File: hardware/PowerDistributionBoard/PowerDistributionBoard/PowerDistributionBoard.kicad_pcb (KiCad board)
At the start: 4 copper layers, 180 x 120 mm, 96 parts, among them J1 Battery, J10 ESC2_PWR, J2 FAN 1, J3 FAN 2, J4 FAN 3, J5 FAN 4, J6 Inverter, J7 Control Board, J8 Conn_01x02, J9 ESC1_PWR, K1 J115F11AH12VDCS61.5, K2 J115F11AH12VDCS61.5, Q1 Q_NMOS_GDS, Q2 Q_NPN_EBC, Q3 Q_NMOS_GSD, Q4 Q_NMOS_GSD, Q5 Q_NPN_EBC, Q6 Q_NMOS_GSD, Q7 Q_NMOS_GSD, Q8 Q_NPN_BEC, SW1 SW_SPDT, U1 LT1641-1, U2 MAX6643LBBAEET, U3 MAX6643LBBAEET, U4 MC74HC20ADG, U5 KSTW004A2B41Z, U6 AP2210N-3.3TRG1

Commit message: Motor Control with ESP/Estop
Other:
- board text added: "OFF"
- board text added: "ON"
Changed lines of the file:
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@@
       (layer "F.Paste" (type "Top Solder Paste"))
       (layer "F.Mask" (type "Top Solder Mask") (thickness 0.01))
-      (layer "F.Cu" (type "copper") (thickness 0.0681))
-      (layer "dielectric 1" (type "core") (thickness 0.469866) (material "FR4") (epsilon_r 4.5) (loss_tangent 0.02))
-      (layer "In1.Cu" (type "copper") (thickness 0.0171))
-      (layer "dielectric 2" (type "prepreg") (thickness 0.469866) (material "FR4") (epsilon_r 4.5) (loss_tangent 0.02))
-      (layer "In2.Cu" (type "copper") (thickness 0.0171))
-      (layer "dielectric 3" (type "core") (thickness 0.469866) (material "FR4") (epsilon_r 4.5) (loss_tangent 0.02))
-      (layer "B.Cu" (type "copper") (thickness 0.0681))
+      (layer "F.Cu" (type "copper") (thickness 0.07))
+      (layer "dielectric 1" (type "core") (thickness 0.456666) (material "FR4") (epsilon_r 4.5) (loss_tangent 0.02))
+      (layer "In1.Cu" (type "copper") (thickness 0.035))
+      (layer "dielectric 2" (type "prepreg") (thickness 0.456666) (material "FR4") (epsilon_r 4.5) (loss_tangent 0.02))
+      (layer "In2.Cu" (type "copper") (thickness 0.035))
+      (layer "dielectric 3" (type "core") (thickness 0.456666) (material "FR4") (epsilon_r 4.5) (loss_tangent 0.02))
+      (layer "B.Cu" (type "copper") (thickness 0.07))
       (layer "B.Mask" (type "Bottom Solder Mask") (thickness 0.01))
       (layer "B.Paste" (type "Bottom Solder Paste"))
@@
       (rotate (xyz 0 0 0))
     )
+    (model "${KIPRJMOD}/Parts/3D Models/436500215.stp"
+      (offset (xyz 1.5 1.9 10))
+      (scale (xyz 1 1 1))
+      (rotate (xyz 90 0 180))
+    )
   )
   (footprint "Resistor_SMD:R_0805_2012Metric" (layer "F.Cu")
@@
       (net 2 "GND") (pinfunction "Pin_2") (pintype "passive"))
     (model "${KICAD6_3DMODEL_DIR}/Connector_Molex.3dshapes/Molex_Mini-Fit_Sr_42820-22XX_1x02_P10.00mm_Horizontal.wrl"
-      (offset (xyz 0 0 0))
+      (offset (xyz 17.25 -5 6.5))
       (scale (xyz 1 1 1))
-      (rotate (xyz 0 0 0))
+      (rotate (xyz -90 0 -90))
+    )
+    (model "${KIPRJMOD}/Parts/3D Models/428202223--3DModel-STEP-390490.STEP"
+      (offset (xyz 17.25 -5 6.5))
+      (scale (xyz 1 1 1))
+      (rotate (xyz -90 0 -90))
     )
   )
@@
     (effects (font (size 1.5 1.5) (thickness 0.3)))
   )
+  (gr_text "ON\n" (at 42.275 84.7) (layer "F.SilkS")
+    (effects (font (size 1 1) (thickness 0.15)))
+  )
   (gr_text "Paradigm IGVC\nPower Distribution Board Rev 1\nDylan Matthews 2023" (at 134.6 44.525) (layer "F.SilkS")
     (effects (font (size 1.5 1.5) (thickness 0.3)))
@@
     (effects (font (size 1.5 1.5) (thickness 0.3)))
   )
+  (gr_text "OFF" (at 42.2 89.925) (layer "F.SilkS")
+    (effects (font (size 1 1) (thickness 0.15)))
+  )
   (gr_text "FANS" (at 183.85 26.5) (layer "F.SilkS")

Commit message: More Control Board Routing Stuff
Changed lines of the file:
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@@
       (effects (font (size 1 1) (thickness 0.15)))
     )
-    (fp_line (start 8 4.5) (end -8 4.5) (layer "F.SilkS") (width 0.12))
-    (fp_line (start -8 -4.5) (end 8 -4.5) (layer "F.SilkS") (width 0.12))
-    (fp_line (start -8 4.5) (end -8 -4.5) (layer "F.SilkS") (width 0.12))
-    (fp_line (start 8 -4.5) (end 8 4.5) (layer "F.SilkS") (width 0.12))
-    (pad "1" smd roundrect (at -5.4 0 180) (size 4.5 8) (layers "F.Cu" "F.Paste" "F.Mask") (roundrect_rratio 0.25)
+    (fp_line (start 8.1 -4.5) (end 8.1 4.5) (layer "F.SilkS") (width 0.12))
+    (fp_line (start 8.1 4.5) (end -8.1 4.5) (layer "F.SilkS") (width 0.12))
+    (fp_line (start -8.1 4.5) (end -8.1 -4.5) (layer "F.SilkS") (width 0.12))
+    (fp_line (start -8.1 -4.5) (end 8.1 -4.5) (layer "F.SilkS") (width 0.12))
+    (pad "1" smd rect (at -5.4 0 180) (size 5.2 8.75) (layers "F.Cu" "F.Paste" "F.Mask")
       (net 28 "Net-(Q1-Pad2)") (pintype "passive"))
-    (pad "2" smd roundrect (at 5.4 0 180) (size 4.5 8) (layers "F.Cu" "F.Paste" "F.Mask") (roundrect_rratio 0.25)
+    (pad "2" smd rect (at 5.4 0 180) (size 5.2 8.75) (layers "F.Cu" "F.Paste" "F.Mask")
       (net 3 "/BATT_RAW") (pintype "passive"))
   )
@@
     (property "Sheetname" "")
     (attr smd)
-    (fp_text reference "Q1" (at 0 -6.65 90) (layer "F.SilkS")
+    (fp_text reference "Q1" (at 9.625 -0.8) (layer "F.SilkS")
       (effects (font (size 1 1) (thickness 0.15)))
     )
@@
         (xy 67.075 77.025)
         (xy 67.101986 80.877896)
-        (xy 59.401986 80.977896)
-        (xy 59.4 67.75)
+        (xy 59.351712 80.977903)
+        (xy 59.349726 67.750007)
         (xy 72.375 57.425)
         (xy 80.563965 57.427856)

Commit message: PDB Layout
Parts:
- removed K1, K2: J115F11AH12VDCS61.5, PDBLib:J115F11AH12VDCS61.5
- added C18: 1u, Capacitor_SMD:C_0805_2012Metric, F.Cu at (85.8, 79.3)
- added C19: 10u, Capacitor_SMD:C_0805_2012Metric, F.Cu at (181.2, 63.2)
- added C20: 1u, Capacitor_SMD:C_0805_2012Metric, F.Cu at (179.1, 63.2)
- added C21: 220uF, Capacitor_THT:CP_Radial_D6.3mm_P2.50mm, F.Cu at (162.6, 59.8)
- added C22: 1u, Capacitor_SMD:C_0805_2012Metric, F.Cu at (179.1, 66.7)
- added C23: 10u, Capacitor_SMD:C_0805_2012Metric, F.Cu at (181.2, 66.7)
- added D10: D, PDBLib:VS-15AWL06FNTR-M3, F.Cu at (182.6, 91.4)
- added D11: S1G, Diode_SMD:D_SMA, F.Cu at (76.6, 115.2)
- added D12: S1G, Diode_SMD:D_SMA, F.Cu at (125.8, 35.4)
- added D13: S1G, Diode_SMD:D_SMA, F.Cu at (209.7, 66.3)
- added D8: S1G, Diode_SMD:D_SMA, F.Cu at (172.7, 34.0)
- added D9: D, PDBLib:VS-15AWL06FNTR-M3, F.Cu at (138.9, 107.7)
- added F2: 10A, PDBLib:3557-2, F.Cu at (143.8, 91.9)
- added F3: 25A, PDBLib:3557-2, F.Cu at (97.7, 110.8)
- added F4: 2A, PDBLib:3557-2, F.Cu at (143.6, 40.2)
- added F5: 10A, PDBLib:3557-2, F.Cu at (167.1, 86.8)
- added F6: 1A, PDBLib:3557-2, F.Cu at (194.6, 66.0)
- added J11: Router, Connector_Molex:Molex_Micro-Fit_3.0_43650-0215_1x02_P3.00mm_Vertical, F.Cu at (217.0, 64.8)
- added Q10: TK100E10N1,S1X, Package_TO_SOT_THT:TO-220-3_Vertical, F.Cu at (164.3, 101.2)
- added Q9: TK100E10N1,S1X, Package_TO_SOT_THT:TO-220-3_Vertical, F.Cu at (119.4, 107.9)
- added R36: 1k, Resistor_SMD:R_0805_2012Metric, F.Cu at (119.4, 116.7)
- added R37: 0, Resistor_SMD:R_2512_6332Metric, F.Cu at (127.5, 105.3)
- added R38: 0, Resistor_SMD:R_2512_6332Metric, F.Cu at (134.9, 98.2)
- added R39: 1k, Resistor_SMD:R_0805_2012Metric, F.Cu at (164.3, 108.0)
- added R40: 0, Resistor_SMD:R_2512_6332Metric, F.Cu at (173.2, 95.5)
- added R41: 0, Resistor_SMD:R_2512_6332Metric, F.Cu at (176.1, 102.3)
- added R42: 100, Resistor_SMD:R_0805_2012Metric, F.Cu at (50.5, 89.7)
- added R43: 100, Resistor_SMD:R_0805_2012Metric, F.Cu at (75.6, 85.3)
- added R44: 4.7k, Resistor_SMD:R_0805_2012Metric, F.Cu at (177.4, 129.7)
- added U7: R-78B9.0-1.0, PDBLib:R-78B9.0-1.0, F.Cu at (171.8, 65.0)
- C1: value 0.68u -> 68n
- C17, C9: footprint Capacitor_THT:CP_Radial_D12.5mm_P5.00mm -> Capacitor_THT:CP_Radial_D10.0mm_P5.00mm
- C3: value 10n -> 1n
- C4: value 1000u -> 220u; footprint Capacitor_THT:CP_Radial_D18.0mm_P7.50mm -> Capacitor_THT:CP_Radial_D16.0mm_P7.50mm
- D2: value D -> SML-P11UTT86R; footprint Diode_SMD:D_SMA -> LED_SMD:LED_0402_1005Metric
- D3: value D -> S1G
- D4, D5: value D -> S1G; footprint Package_TO_SOT_THT:TO-247-2_Horizontal_TabDown -> Diode_SMD:D_SMA
- F1: footprint PDBLib:0679L1000-05 -> PDBLib:3557-2
- J10: value ESC2_PWR -> MOTOR2_PWR
- J7: footprint Connector_Molex:Molex_Micro-Fit_3.0_43650-0200_1x02_P3.00mm_Horizontal -> Connector_Molex:Molex_Micro-Fit_3.0_43650-0215_1x02_P3.00mm_Vertical
- J9: value ESC1_PWR -> MOTOR1_PWR
- Q8: value Q_NPN_BEC -> DMN62D0U-13; footprint Package_TO_SOT_SMD:SOT-23 -> PDBLib:DMN62D0U-13
- R17, R18, R21, R22: value DNP -> 0
- R25: value 360 -> 3.4k
- R3: value 48k -> 46.4k
- R33: value 3k -> 4.7k
- R34: value 0 -> 330
- R35: value DNP -> 1k
- R4: value 0.75m -> 1m
- TP1: value TestPoint -> ON
- TP3: value TestPoint -> ESTOP
- TP4: value TestPoint -> +12V
- moved D3 102.8 mm to (160.9, 34.0), turned to 180 degrees
- moved G*** 95.9 mm to (108.5, 133.5)
- moved J8 93.0 mm to (185.1, 128.8), turned to 90 degrees
- moved D4 92.5 mm to (191.2, 34.0), turned to 180 degrees
- moved TP3 77.0 mm to (180.1, 128.8), turned to 90 degrees
- moved R33 76.9 mm to (175.1, 127.8), turned to 90 degrees
- moved D5 64.6 mm to (203.2, 34.0), turned to 180 degrees
- moved R34 59.7 mm to (171.8, 128.7)
- moved Q8 59.2 mm to (167.6, 127.8), turned to 90 degrees
- moved D2 55.0 mm to (61.0, 89.8), turned to 0 degrees
- moved R35 51.9 mm to (164.3, 128.7), turned to -90 degrees
- moved J9 48.3 mm to (143.7, 116.9), turned to -90 degrees
- moved R25 48.0 mm to (62.1, 92.4), turned to -90 degrees
- moved C16 35.4 mm to (83.7, 79.3)
- moved J7 21.9 mm to (117.7, 36.8), turned to 90 degrees
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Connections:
- net /FAN_FAIL1 renamed /FAN_FAIL1_N
- net /FAN_FAIL2 renamed /FAN_FAIL2_N
- net /OVERTEMP1 renamed /OVERTEMP1_N
- net /OVERTEMP2 renamed /OVERTEMP2_N
- C16 pad 1: /ESTOP -> GND
- C16 pad 2: GND -> +48V
- C17 pad 1: +48V -> Net-(D11-Pad1)
- D1 pad 2: +48V -> Net-(D1-Pad2)
- D2 pad 1: +12V -> Net-(D2-Pad1)
- D2 pad 2: Net-(D2-Pad2) -> /BATT_GOOD
- D3 pad 2: Net-(D2-Pad2) -> Net-(D3-Pad2)
- D4 pad 1: /ESC1_PWR -> +12V
- D4 pad 2: GND -> Net-(D4-Pad2)
- D5 pad 1: /ESC2_PWR -> +12V
- D5 pad 2: GND -> Net-(D5-Pad2)
- F1 pad 1: +48V -> Net-(C9-Pad1)
- F1 pad 2: Net-(C9-Pad1) -> +48V
- J10 pad 1: /ESC2_PWR -> Net-(D10-Pad1)
- J10 pad 2: GND -> Net-(D10-Pad2)
- J2 pad 1: Net-(J2-Pad1) -> Net-(D4-Pad2)
- J3 pad 1: Net-(J3-Pad1) -> Net-(D5-Pad2)
- J4 pad 1: Net-(J4-Pad1) -> Net-(D3-Pad2)
- J5 pad 1: Net-(J5-Pad1) -> Net-(D8-Pad2)
- J6 pad 1: +48V -> Net-(D11-Pad1)
- J7 pad 1: +12V -> Net-(D12-Pad1)
- J8 pad 1: Net-(J8-Pad1) -> /ESTOP
- J9 pad 1: /ESC1_PWR -> Net-(D9-Pad1)
- J9 pad 2: GND -> Net-(D9-Pad2)
- Q8 pad 3: Net-(Q8-Pad3) -> /MOTOR_FET_GATE
- R17 pad 1: Net-(J2-Pad1) -> GND
- R17 pad 2: GND -> Net-(D4-Pad2)
- R18 pad 1: Net-(J4-Pad1) -> GND
- R18 pad 2: GND -> Net-(D3-Pad2)
- R19 pad 1: Net-(J2-Pad1) -> Net-(D4-Pad2)
- R20 pad 1: Net-(J4-Pad1) -> Net-(D3-Pad2)
- R21 pad 1: Net-(J3-Pad1) -> GND
- R21 pad 2: GND -> Net-(D5-Pad2)
- R22 pad 1: Net-(J5-Pad1) -> GND
- R22 pad 2: GND -> Net-(D8-Pad2)
- R23 pad 1: Net-(J3-Pad1) -> Net-(D5-Pad2)
- R24 pad 1: Net-(J5-Pad1) -> Net-(D8-Pad2)
- R25 pad 1: Net-(Q8-Pad1) -> /BATT_GOOD
- R25 pad 2: /ESTOP -> GND
- R33 pad 2: Net-(J8-Pad1) -> +3V3
- R34 pad 1: Net-(Q8-Pad3) -> Net-(Q8-Pad1)
- R34 pad 2: Net-(D2-Pad2) -> /ESTOP
- R35 pad 1: GND -> /MOTOR_FET_GATE
- R35 pad 2: Net-(D2-Pad2) -> +12V
- SW1 pad 3: Net-(C14-Pad1) -> Net-(SW1-Pad3)
- U1 pad 3: /BATT_GOOD -> Net-(D2-Pad1)
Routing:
- net +12V: track 250.6 -> 12.3 mm
- net Net-(D2-Pad2): track 50.8 -> 0.00 mm
- net GND: track 104.4 -> 81.8 mm, vias 96 -> 53
- net /FAN_TACH4: track 21.2 -> 1.03 mm
- net /FAN_TACH2: track 21.0 -> 1.08 mm
- net /FAN_TACH1: track 19.5 -> 0.00 mm
- net /FAN_TACH3: track 19.7 -> 6.72 mm
- net Net-(Q3-Pad1): track 12.7 -> 0.00 mm
- net Net-(R14-Pad1): track 8.08 -> 0.00 mm
- net Net-(J5-Pad1): track 7.84 -> 0.00 mm
- net Net-(J4-Pad1): track 7.75 -> 0.00 mm
- net Net-(J3-Pad1): track 7.74 -> 0.00 mm
- net Net-(C14-Pad1): track 13.7 -> 5.99 mm
- net Net-(J2-Pad1): track 7.61 -> 0.00 mm
- net /ESTOP: track 7.27 -> 0.00 mm
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- removed copper zone on B.Cu, net +12V
- removed copper zone on F.Cu, net +12V
- removed copper zone on B.Cu, net /ESC1_PWR
- removed copper zone on F.Cu, net /ESC1_PWR
- removed copper zone on B.Cu, net /ESC2_PWR
- removed copper zone on F.Cu, net /ESC2_PWR
- removed copper zone on B.Cu, net Net-(C9-Pad1)
- removed copper zone on F.Cu, net Net-(C9-Pad1)
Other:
- board text removed: "CONTROL BOARD"
- board text removed: "ESC1 POWER"
- board text removed: "ESC2 POWER"

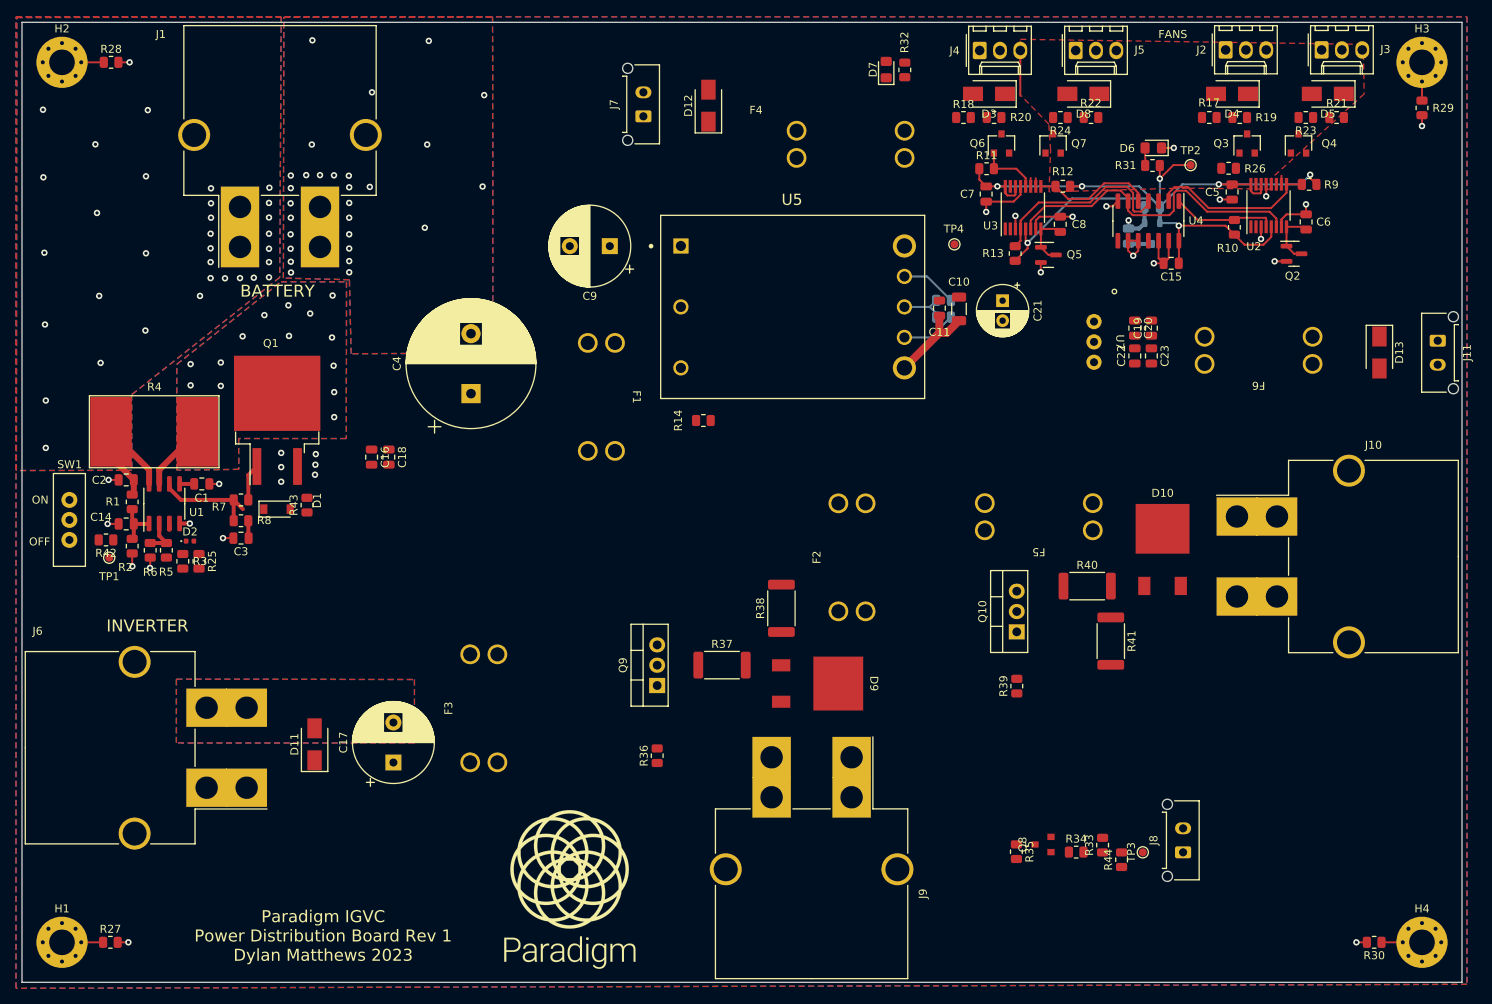
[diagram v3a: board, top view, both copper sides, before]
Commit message: PDB routing V2 first pass
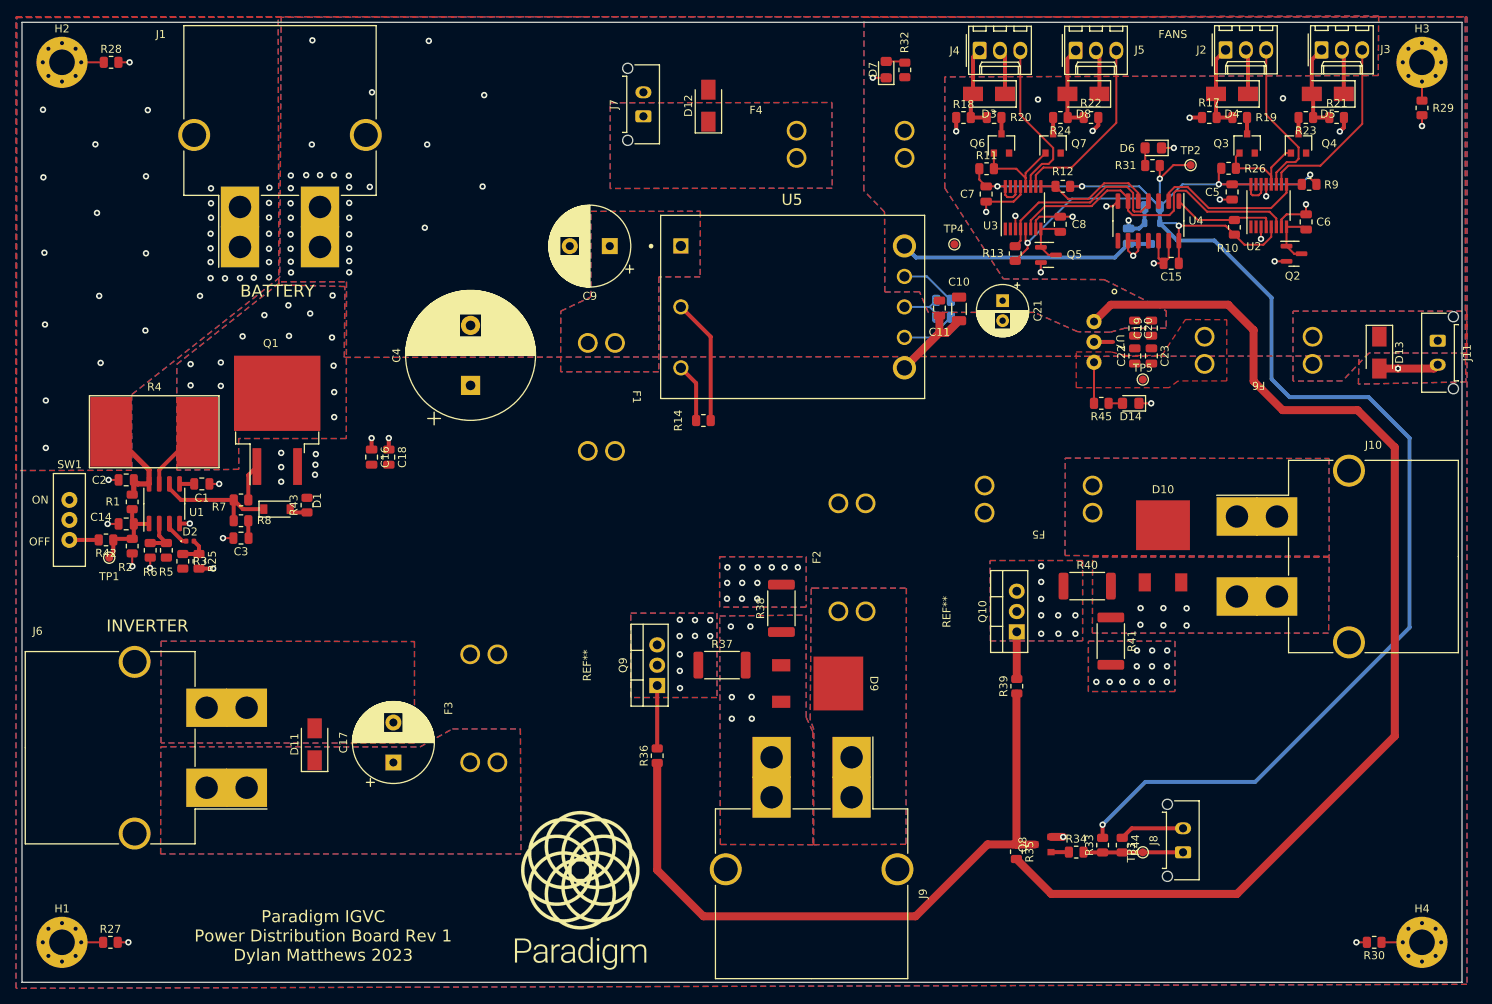
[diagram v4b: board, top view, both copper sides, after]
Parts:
- added D14: Green, LED_SMD:LED_0805_2012Metric_Pad1.15x1.40mm_HandSolder, F.Cu at (178.6, 72.6)
- added R45: 3.6k, Resistor_SMD:R_0805_2012Metric, F.Cu at (174.9, 72.6)
- added REF**: 577102B00000G_HEATSINK, PDBLib:577102B00000G_HEATSINK, F.Cu at (111.1, 105.4)
- added REF**: 577102B00000G_HEATSINK, PDBLib:577102B00000G_HEATSINK, F.Cu at (156.1, 98.7)
- added TP5: +9V, TestPoint:TestPoint_Pad_D1.0mm, F.Cu at (180.1, 69.7)
- moved F5 2.20 mm to (167.1, 84.6)
- moved R44 1.83 mm to (177.5, 127.8), turned to -90 degrees
- moved G*** 1.34 mm to (109.8, 133.6)
- moved C4 1.03 mm to (96.1, 70.4)
- moved D10 0.45 mm to (182.6, 91.0)
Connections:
- net Net-(C9-Pad1) renamed /12VDCDC_48V
- net Net-(D10-Pad1) renamed /MOTOR2_48VA
- net Net-(D10-Pad2) renamed /MOTOR2_48VB
- net Net-(D11-Pad1) renamed /INVERTER_48V
- net Net-(D12-Pad1) renamed /CTRL_12V
- net Net-(D13-Pad1) renamed /ROUTER_9V
- net Net-(D9-Pad1) renamed /MOTOR1_48VA
- net Net-(D9-Pad2) renamed /MOTOR1_48VB
- net Net-(Q1-Pad2) renamed /SENSE
- net Net-(Q10-Pad2) renamed /MOTOR2_48VC
- net Net-(Q9-Pad2) renamed /MOTOR1_48VC
- C13 pad 1: +3.3V -> +3V3
- C15 pad 1: +3.3V -> +3V3
- C5 pad 2: +3.3V -> +3V3
- C7 pad 2: +3.3V -> +3V3
- R10 pad 1: +3.3V -> +3V3
- R11 pad 1: +3.3V -> +3V3
- R12 pad 1: +3.3V -> +3V3
- R13 pad 1: +3.3V -> +3V3
- R26 pad 1: +3.3V -> +3V3
- R31 pad 2: +3.3V -> +3V3
- R9 pad 1: +3.3V -> +3V3
- TP2 pad 1: +3.3V -> +3V3
- U2 pad 14: +3.3V -> +3V3
- U2 pad 16: +3.3V -> +3V3
- U2 pad 5: +3.3V -> +3V3
- U3 pad 14: +3.3V -> +3V3
- U3 pad 16: +3.3V -> +3V3
- U3 pad 5: +3.3V -> +3V3
- U4 pad 14: +3.3V -> +3V3
- U6 pad 2: +3.3V -> +3V3
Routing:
- net +3V3: track 0.00 -> 242.7 mm, vias 0 -> 8
- net +12V: track 12.3 -> 204.8 mm
- net +3.3V: track 117.6 -> 0.00 mm, vias 7 -> 0
- net /MOTOR_FET_GATE: track 0.51 -> 85.6 mm
- net GND: track 81.8 -> 123.7 mm, vias 53 -> 90
- net /FAN_TACH2: track 1.08 -> 23.3 mm
- net /FAN_TACH4: track 1.03 -> 23.2 mm
- net /FAN_TACH1: track 0.00 -> 20.3 mm
- net Net-(R14-Pad1): track 0.00 -> 15.7 mm
- net /FAN_TACH3: track 6.72 -> 20.4 mm
- net Net-(Q3-Pad1): track 0.00 -> 13.3 mm
- net /ESTOP: track 0.00 -> 12.5 mm
- net Net-(D5-Pad2): track 0.00 -> 11.1 mm
- net Net-(D4-Pad2): track 0.00 -> 11.0 mm
- net Net-(D3-Pad2): track 0.00 -> 10.8 mm
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- added copper zone on B.Cu, net +12V
- added copper zone on F.Cu, net +12V
- added copper zone on F.Cu, net +9V
- added copper zone on B.Cu, net /12VDCDC_48V
- added copper zone on F.Cu, net /12VDCDC_48V
- added copper zone on B.Cu, net /CTRL_12V
- added copper zone on F.Cu, net /CTRL_12V
- added copper zone on B.Cu, net /INVERTER_48V
- added copper zone on F.Cu, net /INVERTER_48V
- added copper zone on B.Cu, net /MOTOR1_48VA
- added copper zone on F.Cu, net /MOTOR1_48VA
- added copper zone on B.Cu, net /MOTOR1_48VB
- added copper zone on F.Cu, net /MOTOR1_48VB
- added copper zone on B.Cu, net /MOTOR1_48VC
- added copper zone on F.Cu, net /MOTOR1_48VC
- added copper zone on B.Cu, net /MOTOR2_48VA
- added copper zone on F.Cu, net /MOTOR2_48VA
- added copper zone on B.Cu, net /MOTOR2_48VB
- added copper zone on F.Cu, net /MOTOR2_48VB
- added copper zone on B.Cu, net /MOTOR2_48VC
- added copper zone on F.Cu, net /MOTOR2_48VC
- added copper zone on B.Cu, net /ROUTER_9V
- added copper zone on F.Cu, net /ROUTER_9V

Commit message: Last things
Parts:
- U1: footprint Package_SO:SOIC-8_3.9x4.9mm_P1.27mm -> PDBLib:LT1641-1CS8#TRPBF
- moved U1 0.08 mm to (57.8, 85.2), turned to 0 degrees
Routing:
- net Net-(D2-Pad1): track 4.12 -> 3.26 mm
- net GND: track 123.7 -> 123.9 mm, vias 90 -> 101
- net +48V: vias 6 -> 21
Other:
- board text added: "+9V"
- board text added: "ESTOP"
